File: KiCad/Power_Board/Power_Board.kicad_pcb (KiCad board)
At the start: 4 copper layers, 101.6 x 63.5 mm, 13 parts, among them P1 CONN_LEFT_TOP, P2 CONN_RIGHT_TOP, P3 CONN_LEFT_BOTTOM, P4 CONN_RIGHT_BOTTOM

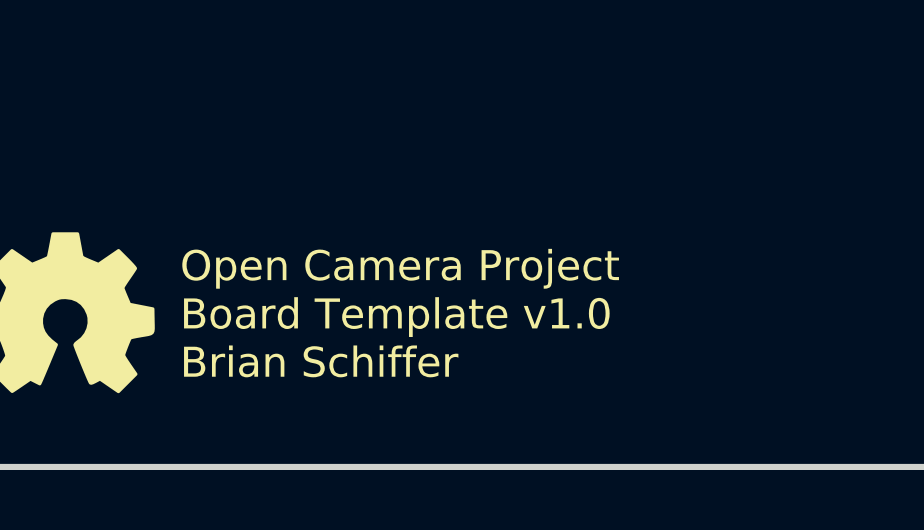
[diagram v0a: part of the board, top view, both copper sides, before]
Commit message: Created TPS63030 footprint.
Also updated PCB sheet.
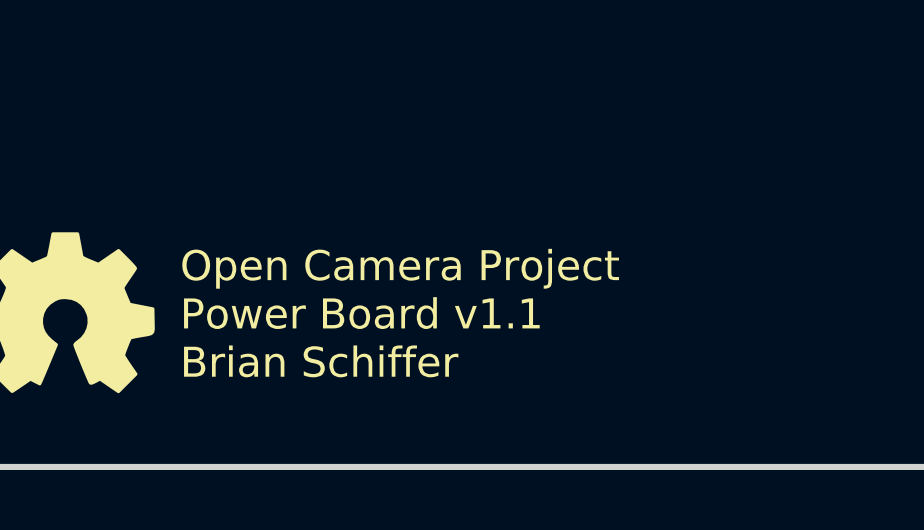
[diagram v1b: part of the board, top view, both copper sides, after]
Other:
- board text added: "Open Camera Project Power Board v1.1 Brian Schiffer"
- board text removed: "Open Camera Project Board Template v1.0 Brian Schiffer"
